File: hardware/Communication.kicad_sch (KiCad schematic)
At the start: 22 parts, among them J7 M80-5100622, T1 HM1193NL, U5 USBLC6-2SC6, U6 MCP2542FD-E/MF, U7 USBLC6-2SC6, U8 MCP2542FD-E/MF

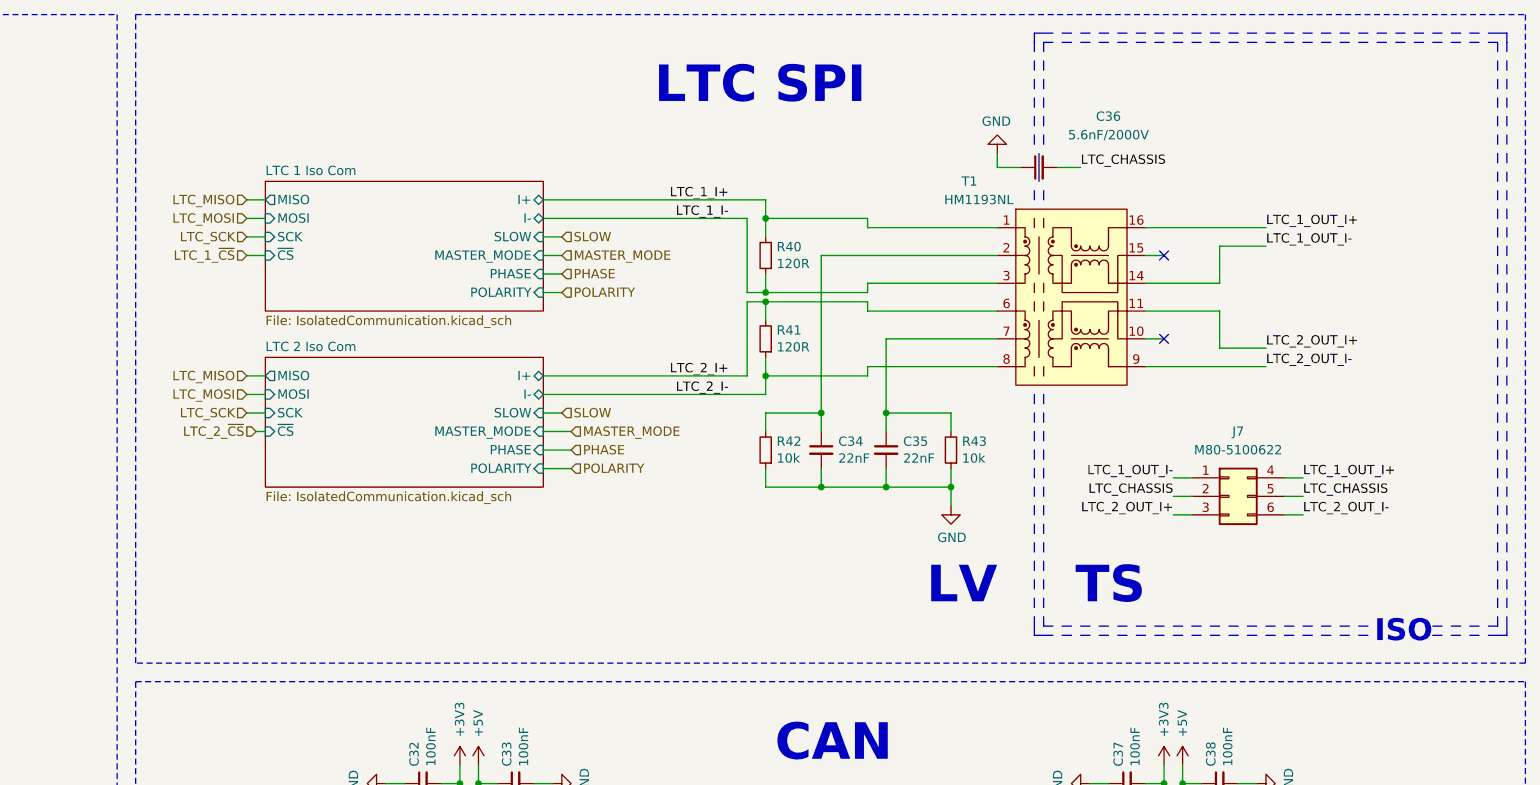
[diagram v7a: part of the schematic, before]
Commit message: fixed some footprints; shorted pcb board to 60x100; re-designed the HV & current measuring as well as LTC communication, all are in one TS section;
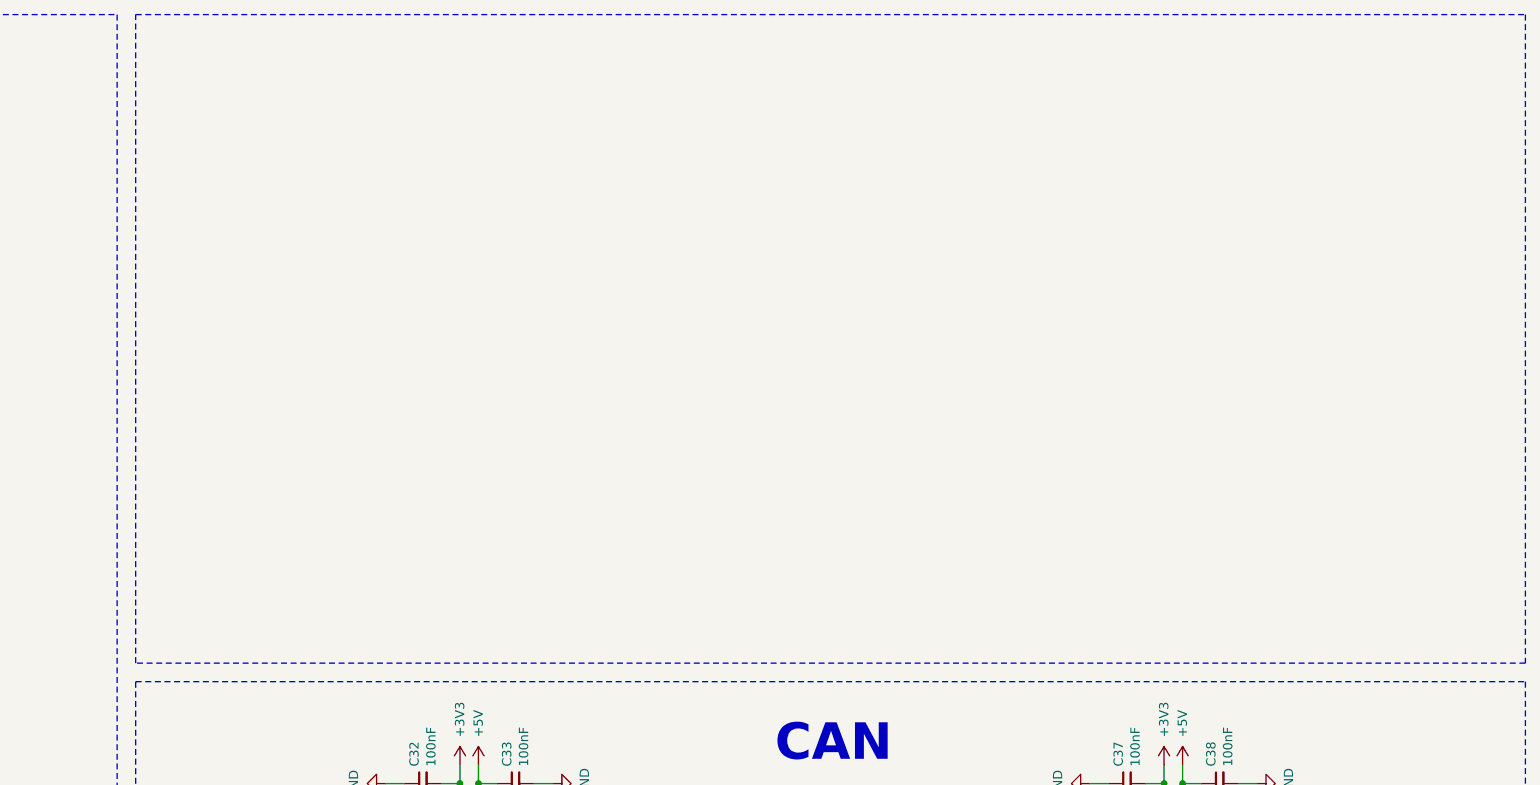
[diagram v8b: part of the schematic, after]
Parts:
- removed C34, C35: 22nF, Capacitor_SMD:C_0603_1608Metric, symbol Device:C_Small
- removed C36: 5.6nF/2000V, Samacsys:C2824, symbol c2824c562jggacauto:C2824C562JGGACAUTO
- removed J7: M80-5100622, Samacsys:M80-51006YY, symbol Samacsys2:M80-5100622
- removed R40, R41: 120R, Resistor_SMD:R_0603_1608Metric, symbol Device:R_Small
- removed R42, R43: 10k, Resistor_SMD:R_0603_1608Metric, symbol Device:R_Small
- removed T1: HM1193NL, Transformer_SMD:Transformer_Pulse_H1100NL, symbol PUTM_EV_BMS_library:HX1188NL
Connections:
- no-connect marks 2 -> 0
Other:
- removed sheet LTC 1 Iso Com
- removed sheet LTC 2 Iso Com
- note removed: "ISO"
- note removed: "LTC SPI"
- note removed: "LV"
- note removed: "TS"
